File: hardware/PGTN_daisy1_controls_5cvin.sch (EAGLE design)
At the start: 81 parts, among them J1 HEADER/MALE/01, J2 HEADER/MALE/01

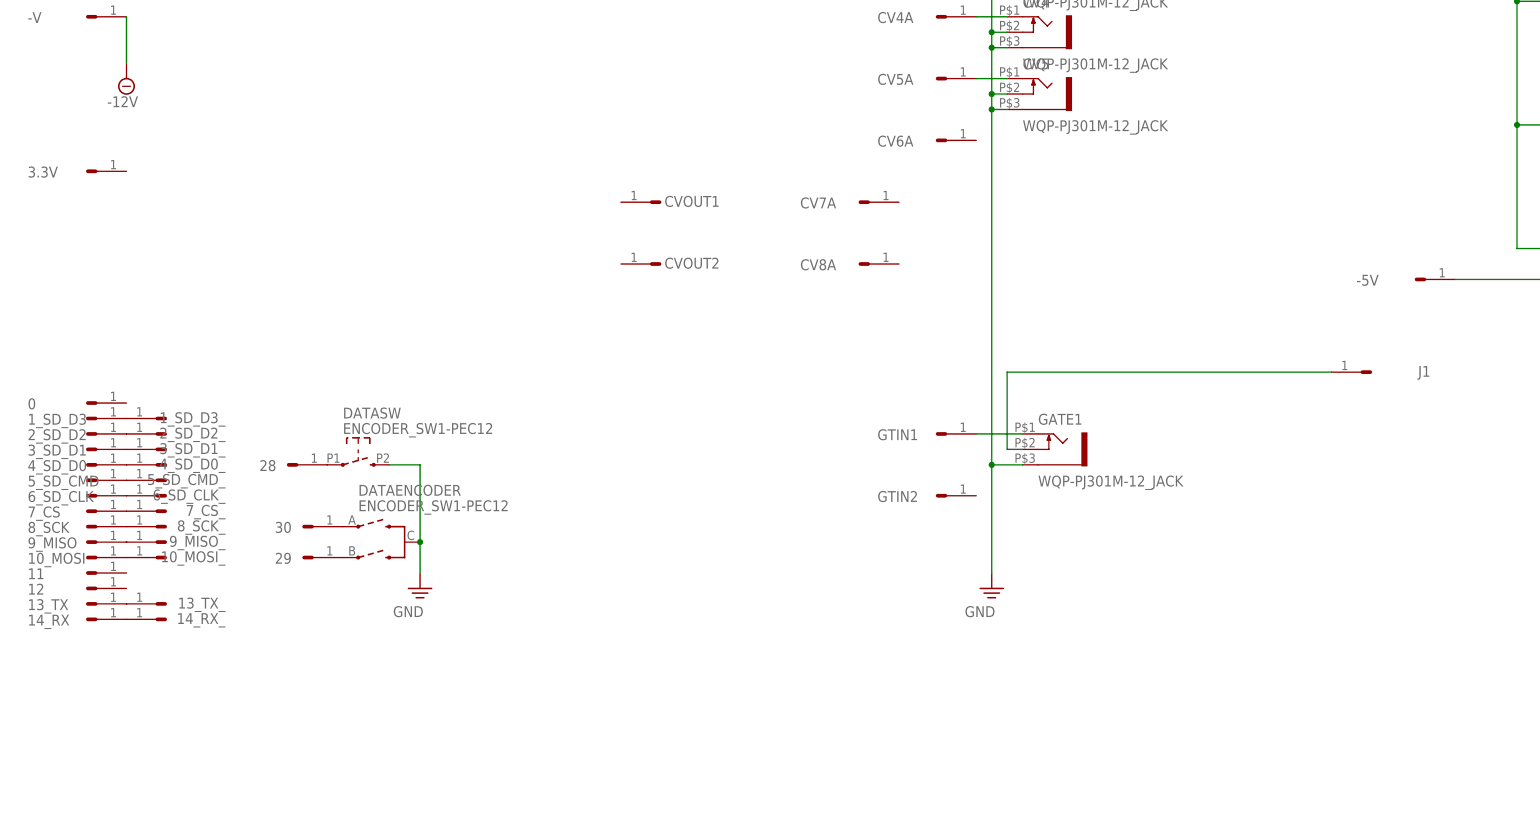
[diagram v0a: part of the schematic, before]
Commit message: Moved UI handling out of controllers
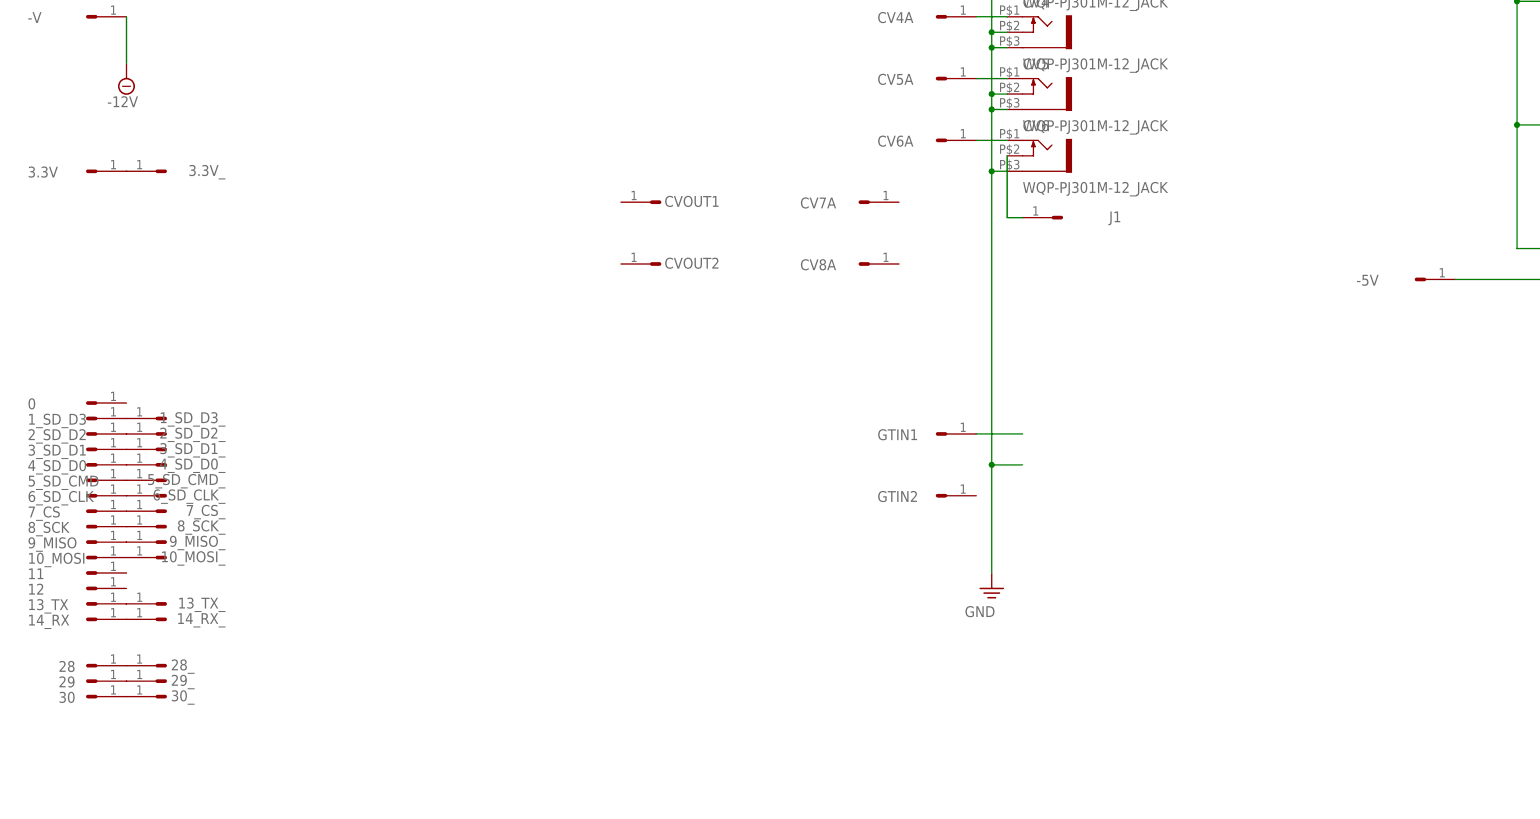
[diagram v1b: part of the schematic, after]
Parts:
- removed DATA: ENCODER_SW1-PEC12, controls:ENCODER_SW1-PEC12
- removed GATE1: WQP-PJ301M-12_JACK, controls:WQP-PJ301M-12_JACK
- added 28_, 29_, 3.3V_, 30_: HEADER/MALE/01, connectors:HEADER/MALE/01
- added CV6: WQP-PJ301M-12_JACK, controls:WQP-PJ301M-12_JACK
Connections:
- removed net N$25: 30.3, DATAENCODER.A
- removed net N$26: 29.3, DATAENCODER.B
- removed net N$27: 28.3, DATASW.1
- removed net N$32: GATE1.3, J1.3
- new net N$10: CV6.2, CV6A.3
- new net N$11: CV6.3, J1.3
- new net N$12: 28.3, 28_.3
- new net N$14: 29.3, 29_.3
- new net N$18: 30.3, 30_.3
- new net N$19: 3.3V.3, 3.3V_.3
- net N$13: no longer GATE1.2
- net PE: now also CV6.1; no longer DATAENCODER.C, DATASW.2, GATE1.1
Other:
- moved on the sheet: 28, 29, 30, J1
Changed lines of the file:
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@@
 <part name="CV5" library="controls" deviceset="WQP-PJ301M-12_JACK" device=""/>
 <part name="SUPPLY8" library="supply" deviceset="GND" device=""/>
-<part name="GATE1" library="controls" deviceset="WQP-PJ301M-12_JACK" device=""/>
 <part name="R1" library="controls" deviceset="9MM_SNAP-IN_POT" device="_"/>
 <part name="R2" library="controls" deviceset="9MM_SNAP-IN_POT" device="_"/>
@@
 <part name="R4" library="controls" deviceset="9MM_SNAP-IN_POT" device="_"/>
 <part name="R5" library="controls" deviceset="9MM_SNAP-IN_POT" device="_"/>
-<part name="DATA" library="controls" deviceset="ENCODER_SW1" device="-PEC12"/>
-<part name="SUPPLY9" library="supply" deviceset="GND" device=""/>
 <part name="10_MOSI_" library="connectors" deviceset="HEADER/MALE/01" device="">
 <attribute name="SPICEPREFIX" value="X"/>
@@
 </part>
 <part name="14_RX_" library="connectors" deviceset="HEADER/MALE/01" device="">
+<attribute name="SPICEPREFIX" value="X"/>
+</part>
+<part name="CV6" library="controls" deviceset="WQP-PJ301M-12_JACK" device=""/>
+<part name="28_" library="connectors" deviceset="HEADER/MALE/01" device="">
+<attribute name="SPICEPREFIX" value="X"/>
+</part>
+<part name="29_" library="connectors" deviceset="HEADER/MALE/01" device="">
+<attribute name="SPICEPREFIX" value="X"/>
+</part>
+<part name="30_" library="connectors" deviceset="HEADER/MALE/01" device="">
+<attribute name="SPICEPREFIX" value="X"/>
+</part>
+<part name="3.3V_" library="connectors" deviceset="HEADER/MALE/01" device="">
 <attribute name="SPICEPREFIX" value="X"/>
 </part>
@@
 <attribute name="NAME" x="217.424" y="85.344" size="1.778" layer="96"/>
 </instance>
-<instance part="28" gate="HEADER" x="48.26" y="-30.48" smashed="yes">
-<attribute name="NAME" x="39.624" y="-31.496" size="1.778" layer="96"/>
-</instance>
-<instance part="29" gate="HEADER" x="50.8" y="-45.72" smashed="yes">
-<attribute name="NAME" x="42.164" y="-46.736" size="1.778" layer="96"/>
-</instance>
-<instance part="30" gate="HEADER" x="50.8" y="-40.64" smashed="yes">
-<attribute name="NAME" x="42.164" y="-41.656" size="1.778" layer="96"/>
+<instance part="28" gate="HEADER" x="15.24" y="-63.5" smashed="yes">
+<attribute name="NAME" x="6.604" y="-64.516" size="1.778" layer="96"/>
+</instance>
+<instance part="29" gate="HEADER" x="15.24" y="-66.04" smashed="yes">
+<attribute name="NAME" x="6.604" y="-67.056" size="1.778" layer="96"/>
+</instance>
+<instance part="30" gate="HEADER" x="15.24" y="-68.58" smashed="yes">
+<attribute name="NAME" x="6.604" y="-69.596" size="1.778" layer="96"/>
 </instance>
 <instance part="-5V" gate="HEADER" x="233.68" y="0" smashed="yes">
@@
 <attribute name="VALUE" x="155.575" y="-55.499" size="1.778" layer="96"/>
 </instance>
-<instance part="GATE1" gate="G$1" x="170.18" y="-27.94" smashed="yes">
-<attribute name="NAME" x="167.64" y="-23.876" size="1.778" layer="95"/>
-<attribute name="VALUE" x="167.64" y="-34.036" size="1.778" layer="96"/>
-</instance>
 <instance part="R1" gate="G$1" x="271.78" y="73.66" smashed="yes" rot="R180">
 <attribute name="NAME" x="276.86" y="76.2" size="1.778" layer="95" rot="R270"/>
@@
 <attribute name="VALUE" x="274.32" y="35.56" size="1.778" layer="96" rot="R270"/>
 </instance>
-<instance part="DATA" gate="ENCODER" x="58.42" y="-43.18" smashed="yes">
-<attribute name="NAME" x="55.88" y="-35.56" size="1.778" layer="95" font="vector"/>
-<attribute name="VALUE" x="55.88" y="-38.1" size="1.778" layer="96" font="vector"/>
-</instance>
-<instance part="SUPPLY9" gate="GND" x="66.04" y="-50.8" smashed="yes">
-<attribute name="VALUE" x="61.595" y="-55.499" size="1.778" layer="96"/>
-</instance>
-<instance part="DATA" gate="SW" x="55.88" y="-27.94" smashed="yes">
-<attribute name="NAME" x="53.34" y="-22.86" size="1.778" layer="95" font="vector"/>
-<attribute name="VALUE" x="53.34" y="-25.4" size="1.778" layer="96" font="vector"/>
-</instance>
 <instance part="10_MOSI_" gate="HEADER" x="20.32" y="-45.72" smashed="yes" rot="R180">
 <attribute name="NAME" x="34.036" y="-44.704" size="1.778" layer="96" rot="R180"/>
@@
 <attribute name="NAME" x="199.644" y="77.724" size="1.778" layer="96"/>
 </instance>
-<instance part="J1" gate="HEADER" x="218.44" y="-15.24" smashed="yes" rot="R180">
-<attribute name="NAME" x="232.156" y="-14.224" size="1.778" layer="96" rot="R180"/>
+<instance part="J1" gate="HEADER" x="167.64" y="10.16" smashed="yes" rot="R180">
+<attribute name="NAME" x="181.356" y="11.176" size="1.778" layer="96" rot="R180"/>
 </instance>
 <instance part="1_SD_D3_" gate="HEADER" x="20.32" y="-22.86" smashed="yes" rot="R180">
@@
 <instance part="14_RX_" gate="HEADER" x="20.32" y="-55.88" smashed="yes" rot="R180">
 <attribute name="NAME" x="34.036" y="-54.864" size="1.778" layer="96" rot="R180"/>
+</instance>
+<instance part="CV6" gate="G$1" x="167.64" y="20.32" smashed="yes">
+<attribute name="NAME" x="165.1" y="24.384" size="1.778" layer="95"/>
+<attribute name="VALUE" x="165.1" y="14.224" size="1.778" layer="96"/>
+</instance>
+<instance part="28_" gate="HEADER" x="20.32" y="-63.5" smashed="yes" rot="R180">
+<attribute name="NAME" x="28.956" y="-62.484" size="1.778" layer="96" rot="R180"/>
+</instance>
+<instance part="29_" gate="HEADER" x="20.32" y="-66.04" smashed="yes" rot="R180">
+<attribute name="NAME" x="28.956" y="-65.024" size="1.778" layer="96" rot="R180"/>
+</instance>
+<instance part="30_" gate="HEADER" x="20.32" y="-68.58" smashed="yes" rot="R180">
+<attribute name="NAME" x="28.956" y="-67.564" size="1.778" layer="96" rot="R180"/>
+</instance>
+<instance part="3.3V_" gate="HEADER" x="20.32" y="17.78" smashed="yes" rot="R180">
+<attribute name="NAME" x="34.036" y="18.796" size="1.778" layer="96" rot="R180"/>
 </instance>
 </instances>
@@
 <segment>
 <pinref part="CV1" gate="G$1" pin="3"/>
-<wire x1="160.02" y1="-30.48" x2="160.02" y2="27.94" width="0.1524" layer="91"/>
+<wire x1="160.02" y1="-30.48" x2="160.02" y2="17.78" width="0.1524" layer="91"/>
+<wire x1="160.02" y1="17.78" x2="160.02" y2="27.94" width="0.1524" layer="91"/>
 <wire x1="160.02" y1="27.94" x2="160.02" y2="30.48" width="0.1524" layer="91"/>
 <wire x1="160.02" y1="30.48" x2="160.02" y2="38.1" width="0.1524" layer="91"/>
@@
 <pinref part="SUPPLY8" gate="GND" pin="PE"/>
 <wire x1="160.02" y1="-30.48" x2="160.02" y2="-48.26" width="0.1524" layer="91"/>
-<pinref part="GATE1" gate="G$1" pin="1"/>
 <wire x1="165.1" y1="-30.48" x2="160.02" y2="-30.48" width="0.1524" layer="91"/>
 <junction x="160.02" y="-30.48"/>
-</segment>
-<segment>
-<pinref part="DATA" gate="ENCODER" pin="C"/>
-<pinref part="SUPPLY9" gate="GND" pin="PE"/>
-<wire x1="66.04" y1="-48.26" x2="66.04" y2="-43.18" width="0.1524" layer="91"/>
-<pinref part="DATA" gate="SW" pin="2"/>
-<wire x1="60.96" y1="-30.48" x2="66.04" y2="-30.48" width="0.1524" layer="91"/>
-<wire x1="66.04" y1="-30.48" x2="66.04" y2="-43.18" width="0.1524" layer="91"/>
-<junction x="66.04" y="-43.18"/>
+<pinref part="CV6" gate="G$1" pin="1"/>
+<wire x1="162.56" y1="17.78" x2="160.02" y2="17.78" width="0.1524" layer="91"/>
+<junction x="160.02" y="17.78"/>
 </segment>
 <segment>
@@
 <net name="N$13" class="0">
 <segment>
-<pinref part="GATE1" gate="G$1" pin="2"/>
 <pinref part="GTIN1" gate="HEADER" pin="3"/>
 <wire x1="165.1" y1="-25.4" x2="157.48" y2="-25.4" width="0.1524" layer="91"/>
@@
 </segment>
 </net>
-<net name="N$25" class="0">
-<segment>
-<pinref part="DATA" gate="ENCODER" pin="A"/>
-<pinref part="30" gate="HEADER" pin="3"/>
-</segment>
-</net>
-<net name="N$26" class="0">
-<segment>
-<pinref part="DATA" gate="ENCODER" pin="B"/>
-<pinref part="29" gate="HEADER" pin="3"/>
-</segment>
-</net>
-<net name="N$27" class="0">
-<segment>
-<pinref part="DATA" gate="SW" pin="1"/>
-<pinref part="28" gate="HEADER" pin="3"/>
-</segment>
-</net>
 <net name="N$28" class="0">
 <segment>
@@
 <pinref part="10_MOSI" gate="HEADER" pin="3"/>
 <pinref part="10_MOSI_" gate="HEADER" pin="3"/>
-</segment>
-</net>
-<net name="N$32" class="0">
-<segment>
-<wire x1="162.56" y1="-15.24" x2="215.9" y2="-15.24" width="0.1524" layer="91"/>
-<pinref part="GATE1" gate="G$1" pin="3"/>
-<wire x1="165.1" y1="-27.94" x2="162.56" y2="-27.94" width="0.1524" layer="91"/>
-<wire x1="162.56" y1="-27.94" x2="162.56" y2="-15.24" width="0.1524" layer="91"/>
-<pinref part="J1" gate="HEADER" pin="3"/>
 </segment>
 </net>
@@
 </segment>
 </net>
+<net name="N$10" class="0">
+<segment>
+<pinref part="CV6A" gate="HEADER" pin="3"/>
+<pinref part="CV6" gate="G$1" pin="2"/>
+<wire x1="157.48" y1="22.86" x2="162.56" y2="22.86" width="0.1524" layer="91"/>
+</segment>
+</net>
+<net name="N$11" class="0">
+<segment>
+<pinref part="J1" gate="HEADER" pin="3"/>
+<pinref part="CV6" gate="G$1" pin="3"/>
+<wire x1="165.1" y1="10.16" x2="162.56" y2="10.16" width="0.1524" layer="91"/>
+<wire x1="162.56" y1="10.16" x2="162.56" y2="20.32" width="0.1524" layer="91"/>
+</segment>
+</net>
+<net name="N$12" class="0">
+<segment>
+<pinref part="28" gate="HEADER" pin="3"/>
+<pinref part="28_" gate="HEADER" pin="3"/>
+</segment>
+</net>
+<net name="N$14" class="0">
+<segment>
+<pinref part="29" gate="HEADER" pin="3"/>
+<pinref part="29_" gate="HEADER" pin="3"/>
+</segment>
+</net>
+<net name="N$18" class="0">
+<segment>
+<pinref part="30" gate="HEADER" pin="3"/>
+<pinref part="30_" gate="HEADER" pin="3"/>
+</segment>
+</net>
+<net name="N$19" class="0">
+<segment>
+<pinref part="3.3V" gate="HEADER" pin="3"/>
+<pinref part="3.3V_" gate="HEADER" pin="3"/>
+</segment>
+</net>
